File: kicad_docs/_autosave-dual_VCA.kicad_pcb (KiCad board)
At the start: 2 copper layers, 45.7 x 99.1 mm, 72 parts, among them J1 signal_in_1, J2 CV_in_1, J3 signal_in_2, J4 CV_in_2, J5 signal_out_1, J6 signal_out_2, J7 power_input, J8 Conn_01x06, J9 Conn_01x06, U1 SSM2164, U2 TL072, U3 TL072, U4 TL072, U5 TL072, U6 MAX6035xxUR50

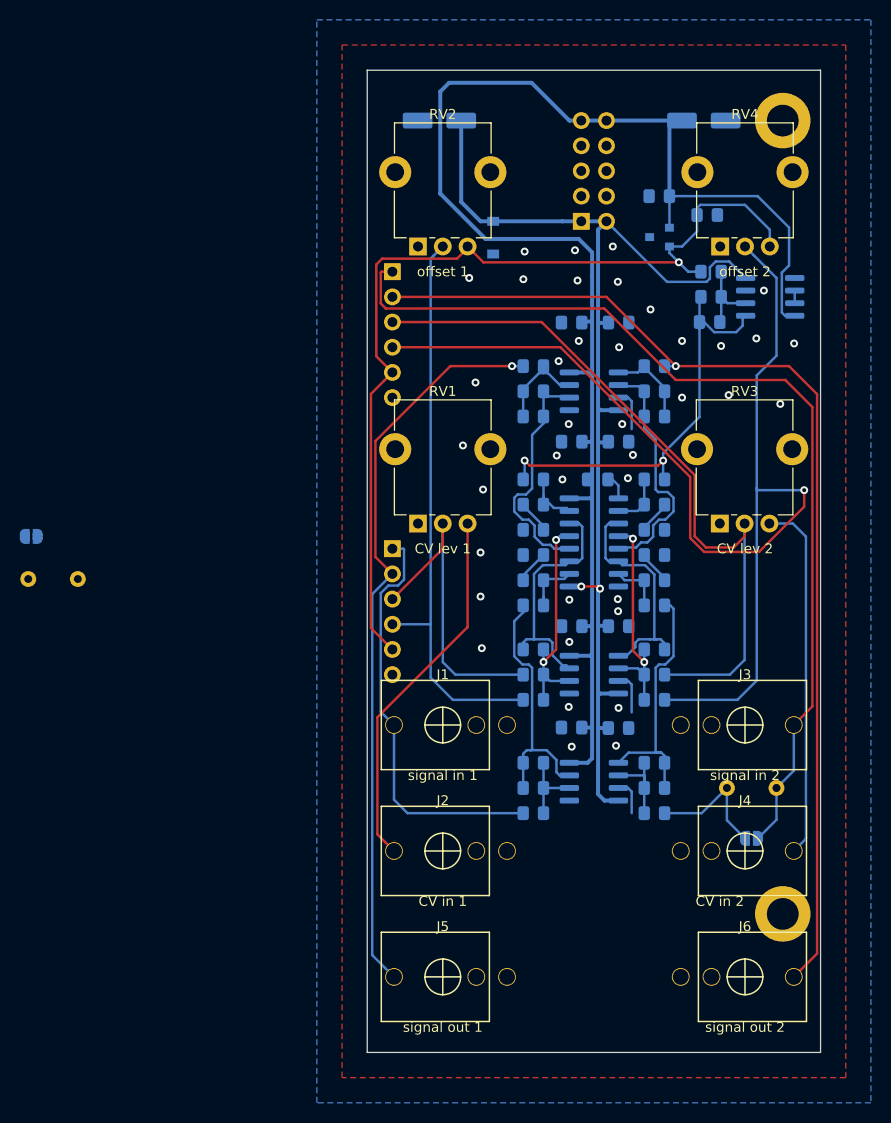
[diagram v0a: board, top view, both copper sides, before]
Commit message: add AC/DC coupling caps and jumper
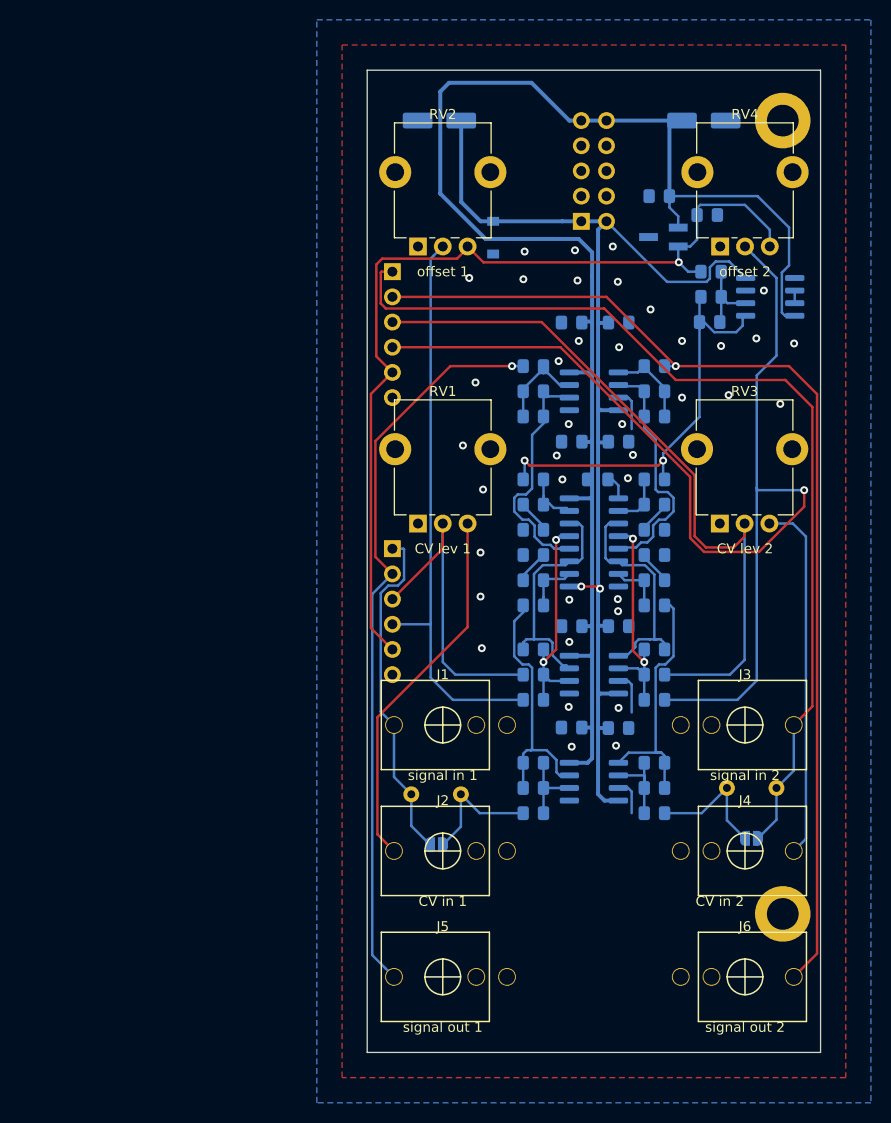
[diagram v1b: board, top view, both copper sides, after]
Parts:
- R1, R3: value R -> 100k
- U6: footprint Package_TO_SOT_SMD:SOT-23 -> Package_TO_SOT_SMD:SOT-23_Handsoldering
- moved JP1 51.4 mm to (78.1, 154.3)
- moved C24 48.7 mm to (80.6, 149.2), turned to 180 degrees
- moved U6 0.39 mm to (101.0, 93.0)
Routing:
- net /VCA_1/VCA_1_signal_v_in: track 0.00 -> 12.9 mm
- net /signal_in_1: track 42.1 -> 34.6 mm
- net +12V: track 153.2 -> 154.2 mm
- net +5VA: track 93.9 -> 93.1 mm
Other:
- board text added: "bridge for DC ch 1"
- board text added: "bridge for DC ch 2"
